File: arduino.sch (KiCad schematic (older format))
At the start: 32 parts, among them J1 USB_C_Receptacle_USB2.0, SW1 ~Reset, U1 FT232RL, U2 ATmega328PB-AU, Y1 Crystal

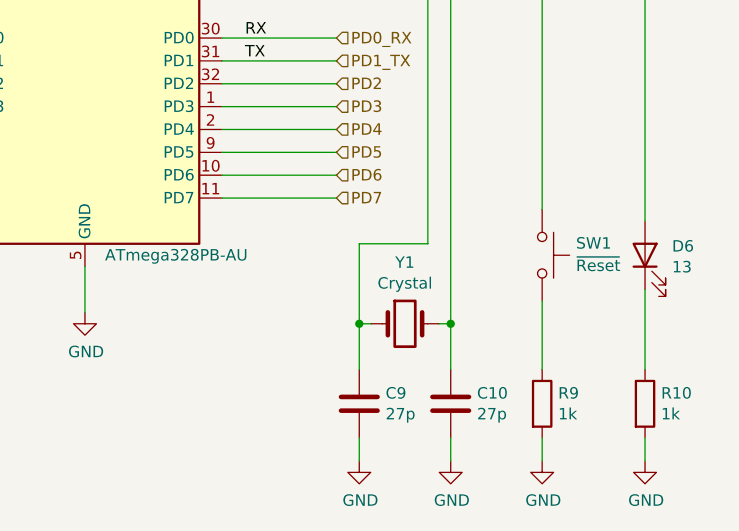
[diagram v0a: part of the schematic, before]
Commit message: Added two 48V digital outputs
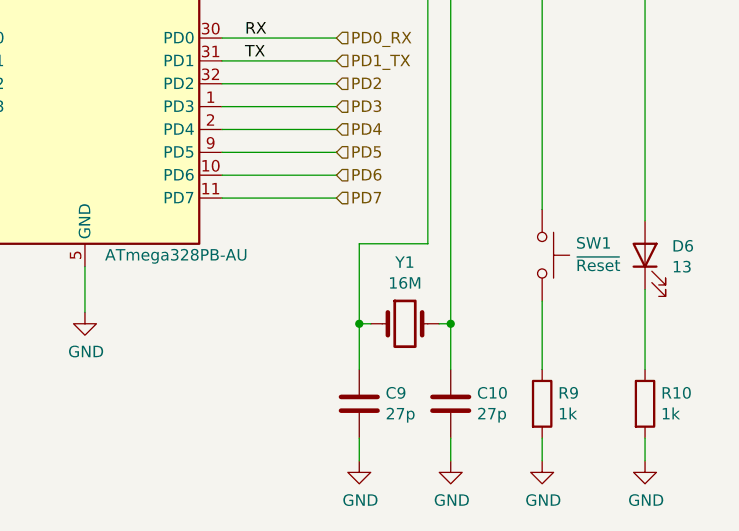
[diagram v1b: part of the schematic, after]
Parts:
- Y1: value Crystal -> 16M
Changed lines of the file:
@@
 $Descr A4 11693 8268
 encoding utf-8
-Sheet 2 2
+Sheet 2 3
 Title "Dumbuino"
 Date "2020-09-20"
@@
 P 9700 5500
 F 0 "Y1" H 9700 5768 50  0000 C CNN
-F 1 "Crystal" H 9700 5677 50  0000 C CNN
+F 1 "16M" H 9700 5677 50  0000 C CNN
 F 2 "" H 9700 5500 50  0001 C CNN
 F 3 "~" H 9700 5500 50  0001 C CNN

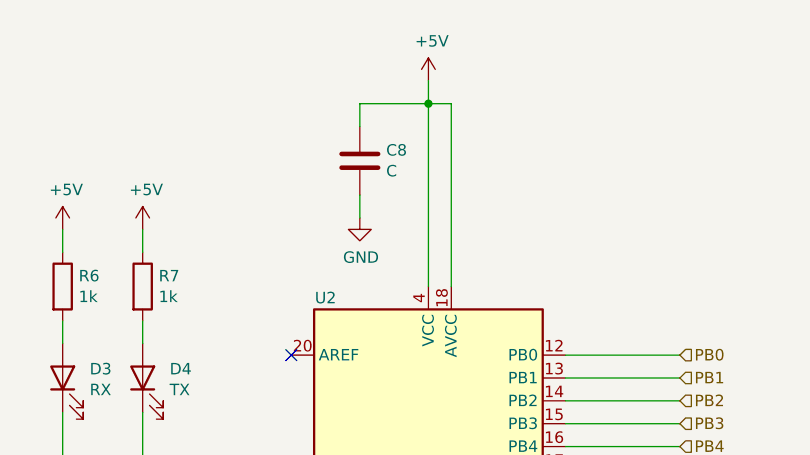
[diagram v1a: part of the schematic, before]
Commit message: Associated footprints
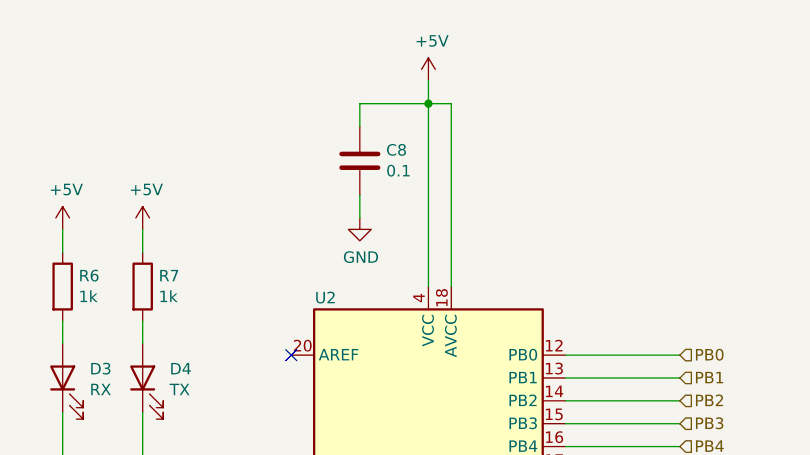
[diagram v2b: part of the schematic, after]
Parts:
- C1, C10, C2, C3, C4, C5, C6, C7, C9: footprint (none) -> Capacitor_SMD:C_0805_2012Metric_Pad1.15x1.40mm_HandSolder
- C8: value C -> 0.1; footprint (none) -> Capacitor_SMD:C_0805_2012Metric_Pad1.15x1.40mm_HandSolder
- D1, D3, D4, D5, D6: footprint (none) -> LED_SMD:LED_0805_2012Metric_Pad1.15x1.40mm_HandSolder
- D2: footprint (none) -> Diode_SMD:D_SOD-123F
- FB1: footprint (none) -> Inductor_SMD:L_0805_2012Metric_Pad1.15x1.40mm_HandSolder
- J1: footprint (none) -> Connector_USB:USB_C_Receptacle_HRO_TYPE-C-31-M-12
- R1, R10, R2, R3, R4, R5, R6, R7, R8, R9: footprint (none) -> Resistor_SMD:R_0805_2012Metric_Pad1.15x1.40mm_HandSolder
- SW1: footprint (none) -> Button_Switch_SMD:SW_SPST_PTS645
- Y1: footprint (none) -> Crystal:Crystal_HC49-U_Vertical
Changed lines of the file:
@@
 F 0 "J1" H 1557 4517 50  0000 C CNN
 F 1 "USB_C_Receptacle_USB2.0" H 1557 4426 50  0000 C CNN
-F 2 "" H 1600 3650 50  0001 C CNN
+F 2 "Connector_USB:USB_C_Receptacle_HRO_TYPE-C-31-M-12" H 1600 3650 50  0001 C CNN
 F 3 "https://www.usb.org/sites/default/files/documents/usb_type-c.zip" H 1600 3650 50  0001 C CNN
 	1    1450 3650
@@
 F 0 "R6" H 6770 2296 50  0000 L CNN
 F 1 "1k" H 6770 2205 50  0000 L CNN
-F 2 "" V 6630 2250 50  0001 C CNN
+F 2 "Resistor_SMD:R_0805_2012Metric_Pad1.15x1.40mm_HandSolder" V 6630 2250 50  0001 C CNN
 F 3 "~" H 6700 2250 50  0001 C CNN
 	1    6700 2250
@@
 F 0 "R7" H 7120 2296 50  0000 L CNN
 F 1 "1k" H 7120 2205 50  0000 L CNN
-F 2 "" V 6980 2250 50  0001 C CNN
+F 2 "Resistor_SMD:R_0805_2012Metric_Pad1.15x1.40mm_HandSolder" V 6980 2250 50  0001 C CNN
 F 3 "~" H 7050 2250 50  0001 C CNN
 	1    7050 2250
@@
 F 0 "R4" H 5720 2796 50  0000 L CNN
 F 1 "1K" H 5720 2705 50  0000 L CNN
-F 2 "" V 5580 2750 50  0001 C CNN
+F 2 "Resistor_SMD:R_0805_2012Metric_Pad1.15x1.40mm_HandSolder" V 5580 2750 50  0001 C CNN
 F 3 "~" H 5650 2750 50  0001 C CNN
 	1    5650 2750
@@
 F 0 "R5" H 5970 3096 50  0000 L CNN
 F 1 "1K" H 5970 3005 50  0000 L CNN
-F 2 "" V 5830 3050 50  0001 C CNN
+F 2 "Resistor_SMD:R_0805_2012Metric_Pad1.15x1.40mm_HandSolder" V 5830 3050 50  0001 C CNN
 F 3 "~" H 5900 3050 50  0001 C CNN
 	1    5900 3050
@@
 F 0 "R8" H 10370 1996 50  0000 L CNN
 F 1 "1k" H 10370 1905 50  0000 L CNN
-F 2 "" V 10230 1950 50  0001 C CNN
+F 2 "Resistor_SMD:R_0805_2012Metric_Pad1.15x1.40mm_HandSolder" V 10230 1950 50  0001 C CNN
 F 3 "~" H 10300 1950 50  0001 C CNN
 	1    10300 1950
@@
 F 0 "R10" H 10820 5896 50  0000 L CNN
 F 1 "1k" H 10820 5805 50  0000 L CNN
-F 2 "" V 10680 5850 50  0001 C CNN
+F 2 "Resistor_SMD:R_0805_2012Metric_Pad1.15x1.40mm_HandSolder" V 10680 5850 50  0001 C CNN
 F 3 "~" H 10750 5850 50  0001 C CNN
 	1    10750 5850
@@
 F 0 "R9" H 10370 5896 50  0000 L CNN
 F 1 "1k" H 10370 5805 50  0000 L CNN
-F 2 "" V 10230 5850 50  0001 C CNN
+F 2 "Resistor_SMD:R_0805_2012Metric_Pad1.15x1.40mm_HandSolder" V 10230 5850 50  0001 C CNN
 F 3 "~" H 10300 5850 50  0001 C CNN
 	1    10300 5850
@@
 F 0 "C2" H 2965 1696 50  0000 L CNN
 F 1 "4u7" H 2965 1605 50  0000 L CNN
-F 2 "" H 2888 1500 50  0001 C CNN
+F 2 "Capacitor_SMD:C_0805_2012Metric_Pad1.15x1.40mm_HandSolder" H 2888 1500 50  0001 C CNN
 F 3 "~" H 2850 1650 50  0001 C CNN
 	1    2850 1650
@@
 F 0 "C3" H 3365 1696 50  0000 L CNN
 F 1 "0.1" H 3365 1605 50  0000 L CNN
-F 2 "" H 3288 1500 50  0001 C CNN
+F 2 "Capacitor_SMD:C_0805_2012Metric_Pad1.15x1.40mm_HandSolder" H 3288 1500 50  0001 C CNN
 F 3 "~" H 3250 1650 50  0001 C CNN
 	1    3250 1650
@@
 F 0 "C5" H 4465 2496 50  0000 L CNN
 F 1 "0.1" H 4465 2405 50  0000 L CNN
-F 2 "" H 4388 2300 50  0001 C CNN
+F 2 "Capacitor_SMD:C_0805_2012Metric_Pad1.15x1.40mm_HandSolder" H 4388 2300 50  0001 C CNN
 F 3 "~" H 4350 2450 50  0001 C CNN
 	1    4350 2450
@@
 F 0 "C6" H 5265 2496 50  0000 L CNN
 F 1 "0.1" H 5265 2405 50  0000 L CNN
-F 2 "" H 5188 2300 50  0001 C CNN
+F 2 "Capacitor_SMD:C_0805_2012Metric_Pad1.15x1.40mm_HandSolder" H 5188 2300 50  0001 C CNN
 F 3 "~" H 5150 2450 50  0001 C CNN
 	1    5150 2450
@@
 F 0 "C4" H 3615 4796 50  0000 L CNN
 F 1 "0.1" H 3615 4705 50  0000 L CNN
-F 2 "" H 3538 4600 50  0001 C CNN
+F 2 "Capacitor_SMD:C_0805_2012Metric_Pad1.15x1.40mm_HandSolder" H 3538 4600 50  0001 C CNN
 F 3 "~" H 3500 4750 50  0001 C CNN
 	1    3500 4750
@@
 F 0 "C1" H 2915 2746 50  0000 L CNN
 F 1 "0.01" H 2915 2655 50  0000 L CNN
-F 2 "" H 2838 2550 50  0001 C CNN
+F 2 "Capacitor_SMD:C_0805_2012Metric_Pad1.15x1.40mm_HandSolder" H 2838 2550 50  0001 C CNN
 F 3 "~" H 2800 2700 50  0001 C CNN
 	1    2800 2700
@@
 F 0 "C9" H 9615 5896 50  0000 L CNN
 F 1 "27p" H 9615 5805 50  0000 L CNN
-F 2 "" H 9538 5700 50  0001 C CNN
+F 2 "Capacitor_SMD:C_0805_2012Metric_Pad1.15x1.40mm_HandSolder" H 9538 5700 50  0001 C CNN
 F 3 "~" H 9500 5850 50  0001 C CNN
 	1    9500 5850
@@
 F 0 "C10" H 10015 5896 50  0000 L CNN
 F 1 "27p" H 10015 5805 50  0000 L CNN
-F 2 "" H 9938 5700 50  0001 C CNN
+F 2 "Capacitor_SMD:C_0805_2012Metric_Pad1.15x1.40mm_HandSolder" H 9938 5700 50  0001 C CNN
 F 3 "~" H 9900 5850 50  0001 C CNN
 	1    9900 5850
@@
 P 8000 1700
 F 0 "C8" H 8115 1746 50  0000 L CNN
-F 1 "C" H 8115 1655 50  0000 L CNN
-F 2 "" H 8038 1550 50  0001 C CNN
+F 1 "0.1" H 8115 1655 50  0000 L CNN
+F 2 "Capacitor_SMD:C_0805_2012Metric_Pad1.15x1.40mm_HandSolder" H 8038 1550 50  0001 C CNN
 F 3 "~" H 8000 1700 50  0001 C CNN
 	1    8000 1700
@@
 F 0 "C7" H 6035 3304 50  0000 R CNN
 F 1 "0.1" H 6035 3395 50  0000 R CNN
-F 2 "" H 6188 3200 50  0001 C CNN
+F 2 "Capacitor_SMD:C_0805_2012Metric_Pad1.15x1.40mm_HandSolder" H 6188 3200 50  0001 C CNN
 F 3 "~" H 6150 3350 50  0001 C CNN
 	1    6150 3350
@@
 F 0 "Y1" H 9700 5768 50  0000 C CNN
 F 1 "16M" H 9700 5677 50  0000 C CNN
-F 2 "" H 9700 5500 50  0001 C CNN
+F 2 "Crystal:Crystal_HC49-U_Vertical" H 9700 5500 50  0001 C CNN
 F 3 "~" H 9700 5500 50  0001 C CNN
 	1    9700 5500
@@
 F 0 "SW1" V 10248 5348 50  0000 L CNN
 F 1 "~Reset" V 10346 5348 50  0000 L CNN
-F 2 "" H 10300 5400 50  0001 C CNN
+F 2 "Button_Switch_SMD:SW_SPST_PTS645" H 10300 5400 50  0001 C CNN
 F 3 "~" H 10300 5400 50  0001 C CNN
 	1    10300 5200
@@
 F 0 "D2" H 2450 1967 50  0000 C CNN
 F 1 "D_Schottky" H 2450 1876 50  0000 C CNN
-F 2 "" H 2450 1750 50  0001 C CNN
+F 2 "Diode_SMD:D_SOD-123F" H 2450 1750 50  0001 C CNN
 F 3 "~" H 2450 1750 50  0001 C CNN
 	1    2450 1750
@@
 F 0 "FB1" H 2587 2196 50  0000 L CNN
 F 1 "600" H 2587 2105 50  0000 L CNN
-F 2 "" V 2380 2150 50  0001 C CNN
+F 2 "Inductor_SMD:L_0805_2012Metric_Pad1.15x1.40mm_HandSolder" V 2380 2150 50  0001 C CNN
 F 3 "~" H 2450 2150 50  0001 C CNN
 	1    2450 2150
@@
 F 0 "D1" V 1539 1832 50  0000 R CNN
 F 1 "PWR" V 1448 1832 50  0000 R CNN
-F 2 "" H 1500 1950 50  0001 C CNN
+F 2 "LED_SMD:LED_0805_2012Metric_Pad1.15x1.40mm_HandSolder" H 1500 1950 50  0001 C CNN
 F 3 "~" H 1500 1950 50  0001 C CNN
 	1    1500 1950
@@
 F 0 "D4" V 7089 2532 50  0000 R CNN
 F 1 "TX" V 6998 2532 50  0000 R CNN
-F 2 "" H 7050 2650 50  0001 C CNN
+F 2 "LED_SMD:LED_0805_2012Metric_Pad1.15x1.40mm_HandSolder" H 7050 2650 50  0001 C CNN
 F 3 "~" H 7050 2650 50  0001 C CNN
 	1    7050 2650
@@
 F 0 "D5" V 10339 2282 50  0000 R CNN
 F 1 "Reset" V 10248 2282 50  0000 R CNN
-F 2 "" H 10300 2400 50  0001 C CNN
+F 2 "LED_SMD:LED_0805_2012Metric_Pad1.15x1.40mm_HandSolder" H 10300 2400 50  0001 C CNN
 F 3 "~" H 10300 2400 50  0001 C CNN
 	1    10300 2400
@@
 F 0 "R1" H 1570 1596 50  0000 L CNN
 F 1 "1k" H 1570 1505 50  0000 L CNN
-F 2 "" V 1430 1550 50  0001 C CNN
+F 2 "Resistor_SMD:R_0805_2012Metric_Pad1.15x1.40mm_HandSolder" V 1430 1550 50  0001 C CNN
 F 3 "~" H 1500 1550 50  0001 C CNN
 	1    1500 1550
@@
 F 0 "R3" H 2920 4796 50  0000 L CNN
 F 1 "5.11k" H 2920 4705 50  0000 L CNN
-F 2 "" V 2780 4750 50  0001 C CNN
+F 2 "Resistor_SMD:R_0805_2012Metric_Pad1.15x1.40mm_HandSolder" V 2780 4750 50  0001 C CNN
 F 3 "~" H 2850 4750 50  0001 C CNN
 	1    2850 4750
@@
 F 0 "R2" H 2520 4796 50  0000 L CNN
 F 1 "5.11k" H 2520 4705 50  0000 L CNN
-F 2 "" V 2380 4750 50  0001 C CNN
+F 2 "Resistor_SMD:R_0805_2012Metric_Pad1.15x1.40mm_HandSolder" V 2380 4750 50  0001 C CNN
 F 3 "~" H 2450 4750 50  0001 C CNN
 	1    2450 4750
@@
 F 0 "D3" V 6739 2532 50  0000 R CNN
 F 1 "RX" V 6648 2532 50  0000 R CNN
-F 2 "" H 6700 2650 50  0001 C CNN
+F 2 "LED_SMD:LED_0805_2012Metric_Pad1.15x1.40mm_HandSolder" H 6700 2650 50  0001 C CNN
 F 3 "~" H 6700 2650 50  0001 C CNN
 	1    6700 2650
@@
 F 0 "D6" V 10789 5082 50  0000 R CNN
 F 1 "13" V 10698 5082 50  0000 R CNN
-F 2 "" H 10750 5200 50  0001 C CNN
+F 2 "LED_SMD:LED_0805_2012Metric_Pad1.15x1.40mm_HandSolder" H 10750 5200 50  0001 C CNN
 F 3 "~" H 10750 5200 50  0001 C CNN
 	1    10750 5200

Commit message: Updated values
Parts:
- C1: value 0.01 -> 0.01u
- C3, C4, C5, C6, C7, C8: value 0.1 -> 0.1u
- J1: symbol Connector:USB_C_Receptacle_USB2.0 -> dumbuino-rescue:USB_C_Receptacle_USB2.0-Connector
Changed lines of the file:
@@
 $EndDescr
 $Comp
-L Connector:USB_C_Receptacle_USB2.0 J1
+L dumbuino-rescue:USB_C_Receptacle_USB2.0-Connector J1
 U 1 1 5F67841E
 P 1450 3650
+AR Path="/5F67841E" Ref="J1"  Part="1"
+AR Path="/5F673CBC/5F67841E" Ref="J1"  Part="1"
 F 0 "J1" H 1557 4517 50  0000 C CNN
 F 1 "USB_C_Receptacle_USB2.0" H 1557 4426 50  0000 C CNN
@@
 P 3250 1650
 F 0 "C3" H 3365 1696 50  0000 L CNN
-F 1 "0.1" H 3365 1605 50  0000 L CNN
+F 1 "0.1u" H 3365 1605 50  0000 L CNN
 F 2 "Capacitor_SMD:C_0805_2012Metric_Pad1.15x1.40mm_HandSolder" H 3288 1500 50  0001 C CNN
 F 3 "~" H 3250 1650 50  0001 C CNN
@@
 P 4350 2450
 F 0 "C5" H 4465 2496 50  0000 L CNN
-F 1 "0.1" H 4465 2405 50  0000 L CNN
+F 1 "0.1u" H 4465 2405 50  0000 L CNN
 F 2 "Capacitor_SMD:C_0805_2012Metric_Pad1.15x1.40mm_HandSolder" H 4388 2300 50  0001 C CNN
 F 3 "~" H 4350 2450 50  0001 C CNN
@@
 P 5150 2450
 F 0 "C6" H 5265 2496 50  0000 L CNN
-F 1 "0.1" H 5265 2405 50  0000 L CNN
+F 1 "0.1u" H 5265 2405 50  0000 L CNN
 F 2 "Capacitor_SMD:C_0805_2012Metric_Pad1.15x1.40mm_HandSolder" H 5188 2300 50  0001 C CNN
 F 3 "~" H 5150 2450 50  0001 C CNN
@@
 P 3500 4750
 F 0 "C4" H 3615 4796 50  0000 L CNN
-F 1 "0.1" H 3615 4705 50  0000 L CNN
+F 1 "0.1u" H 3615 4705 50  0000 L CNN
 F 2 "Capacitor_SMD:C_0805_2012Metric_Pad1.15x1.40mm_HandSolder" H 3538 4600 50  0001 C CNN
 F 3 "~" H 3500 4750 50  0001 C CNN
@@
 P 2800 2700
 F 0 "C1" H 2915 2746 50  0000 L CNN
-F 1 "0.01" H 2915 2655 50  0000 L CNN
+F 1 "0.01u" H 2915 2655 50  0000 L CNN
 F 2 "Capacitor_SMD:C_0805_2012Metric_Pad1.15x1.40mm_HandSolder" H 2838 2550 50  0001 C CNN
 F 3 "~" H 2800 2700 50  0001 C CNN
@@
 P 8000 1700
 F 0 "C8" H 8115 1746 50  0000 L CNN
-F 1 "0.1" H 8115 1655 50  0000 L CNN
+F 1 "0.1u" H 8115 1655 50  0000 L CNN
 F 2 "Capacitor_SMD:C_0805_2012Metric_Pad1.15x1.40mm_HandSolder" H 8038 1550 50  0001 C CNN
 F 3 "~" H 8000 1700 50  0001 C CNN
@@
 P 6150 3350
 F 0 "C7" H 6035 3304 50  0000 R CNN
-F 1 "0.1" H 6035 3395 50  0000 R CNN
+F 1 "0.1u" H 6035 3395 50  0000 R CNN
 F 2 "Capacitor_SMD:C_0805_2012Metric_Pad1.15x1.40mm_HandSolder" H 6188 3200 50  0001 C CNN
 F 3 "~" H 6150 3350 50  0001 C CNN
